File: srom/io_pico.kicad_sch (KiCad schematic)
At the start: 2 parts, among them J201 Conn_01x03_Female, U201 Pico-2 IO

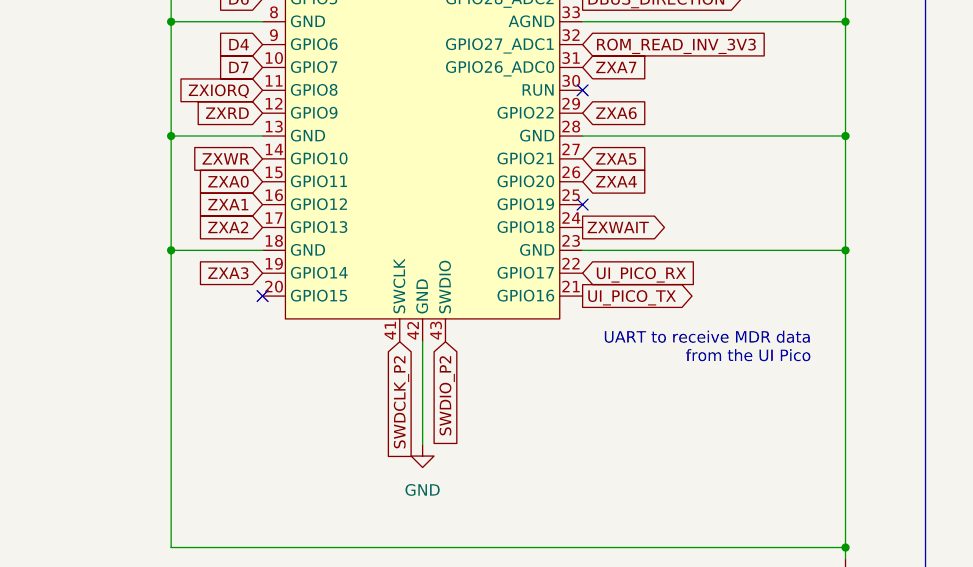
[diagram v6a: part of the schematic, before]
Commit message: move the ZXWAIT signal on pico2 off the SP1 connection. matches latest hardware
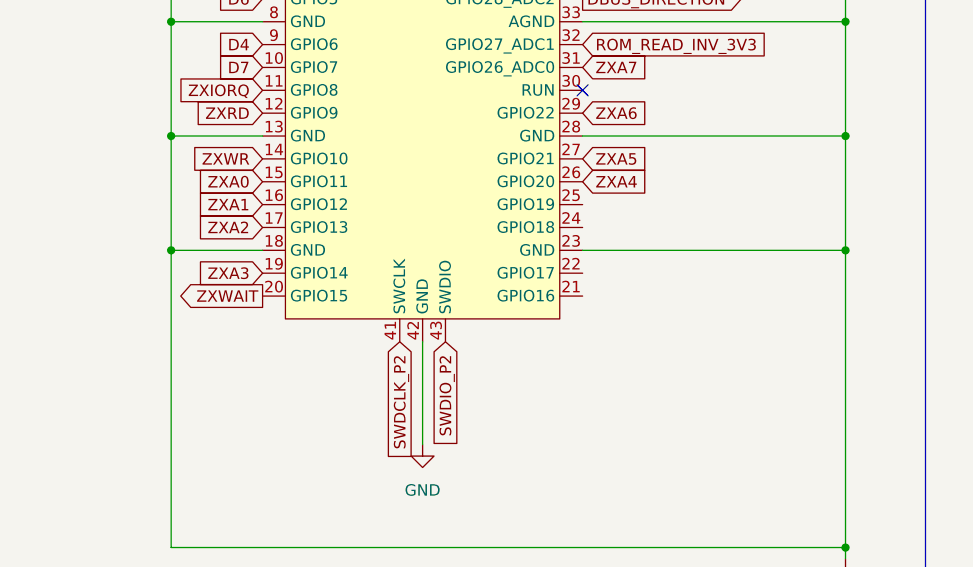
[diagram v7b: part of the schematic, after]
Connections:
- net ZXWAIT: now also U201.20 (GPIO15); no longer U201.24 (GPIO18)
- net UI_PICO_RX: no longer names the net of U201.22 (GPIO17)
- net UI_PICO_TX: no longer names the net of U201.21 (GPIO16)
- no-connect marks 6 -> 4
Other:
- note removed: "UART to receive MDR data from the UI Pico"
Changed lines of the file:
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@@
   )
   (no_connect (at 162.56 49.53))
-  (no_connect (at 127 97.79))
   (no_connect (at 162.56 62.23))
   (no_connect (at 162.56 57.15))
-  (no_connect (at 162.56 87.63))
   (no_connect (at 162.56 74.93))
   (polyline (pts (xy 95.25 155.575) (xy 95.25 35.56))
@@
     (stroke (width 0) (type default) (color 0 0 0 0))
   )
-  (text "UART to receive MDR data\nfrom the UI Pico" (at 187.96 105.41 180)
-    (effects (font (size 1.27 1.27)) (justify right bottom))
-  )
   (text "Pico watches the /IORQ waiting for a Z80 IN or OUT. It knows which from the /RD and /WR lines.\nIt only needs the lower 8 bits of the address bus, and loads the result onto the data bus lines.\n\nThis Pico does the data bus level shifter direction change for both a memory read and an IO\nread. The PIO program which changes the level shifter (BUS_DIRECTION) runs here. That's why\nROM_READ_INV is required as an input here.\n\n/WAIT is output from here to the Z80 when the Pico code needs the Z80 to wait while the byte\nfor the microdrive is dealt with.\n\nMDR data will come in from the UI Pico via UART.\n"
     (at 96.52 154.94 0)
@@
     (property "Intersheet References" "${INTERSHEET_REFS}" (id 0) (at 119.8698 85.0106 0)
       (effects (font (size 1.27 1.27)) (justify right) hide)
-    )
-  )
-  (global_label "UI_PICO_RX" (shape input) (at 162.56 95.25 0) (fields_autoplaced)
-    (effects (font (size 1.27 1.27)) (justify left))
-    (property "Intersheet References" "${INTERSHEET_REFS}" (id 0) (at 175.7983 95.1706 0)
-      (effects (font (size 1.27 1.27)) (justify left) hide)
     )
   )
@@
     (effects (font (size 1.27 1.27)) (justify left))
     (property "Intersheet References" "${INTERSHEET_REFS}" (id 0) (at 192.1874 51.9906 0)
-      (effects (font (size 1.27 1.27)) (justify left) hide)
-    )
-  )
-  (global_label "UI_PICO_TX" (shape output) (at 162.56 97.79 0) (fields_autoplaced)
-    (effects (font (size 1.27 1.27)) (justify left))
-    (property "Intersheet References" "${INTERSHEET_REFS}" (id 0) (at 175.496 97.7106 0)
       (effects (font (size 1.27 1.27)) (justify left) hide)
     )
@@
     )
   )
-  (global_label "ZXWAIT" (shape output) (at 162.56 90.17 0) (fields_autoplaced)
-    (effects (font (size 1.27 1.27)) (justify left))
-    (property "Intersheet References" "${INTERSHEET_REFS}" (id 0) (at 171.5045 90.0906 0)
-      (effects (font (size 1.27 1.27)) (justify left) hide)
+  (global_label "ZXWAIT" (shape output) (at 127 97.79 180) (fields_autoplaced)
+    (effects (font (size 1.27 1.27)) (justify right))
+    (property "Intersheet References" "${INTERSHEET_REFS}" (id 0) (at 118.0555 97.8694 0)
+      (effects (font (size 1.27 1.27)) (justify right) hide)
     )
   )

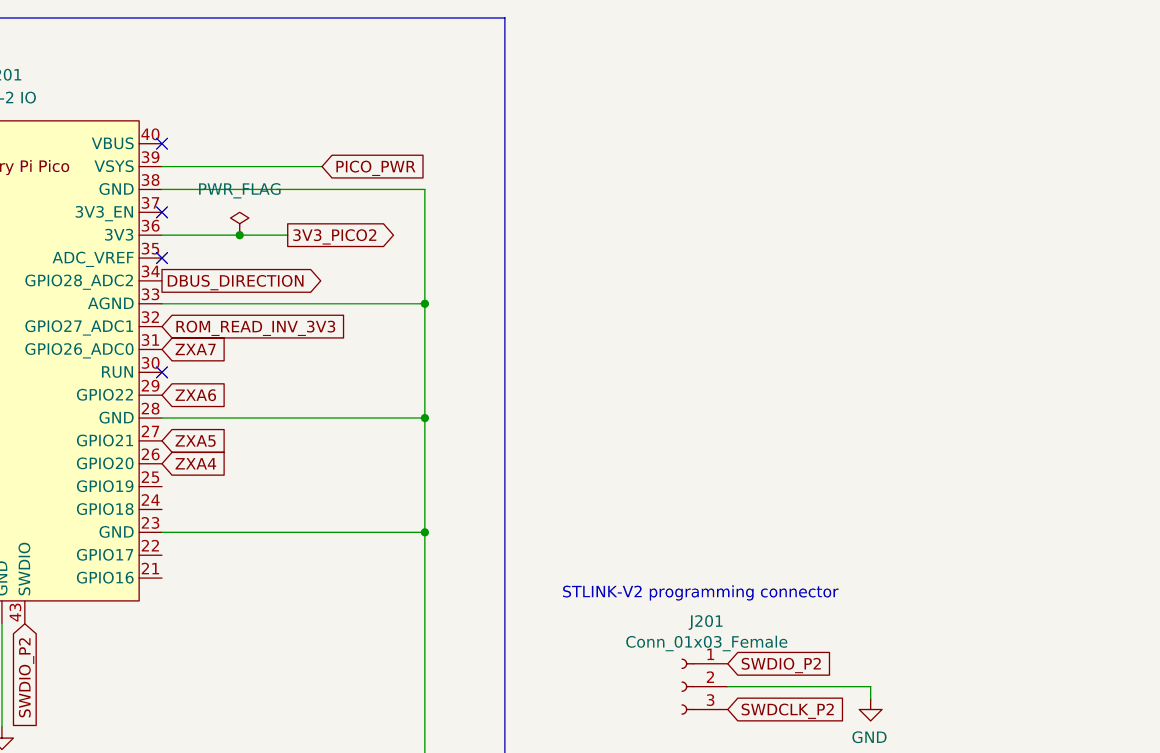
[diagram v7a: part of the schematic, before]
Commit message: update schematic to match current hardware
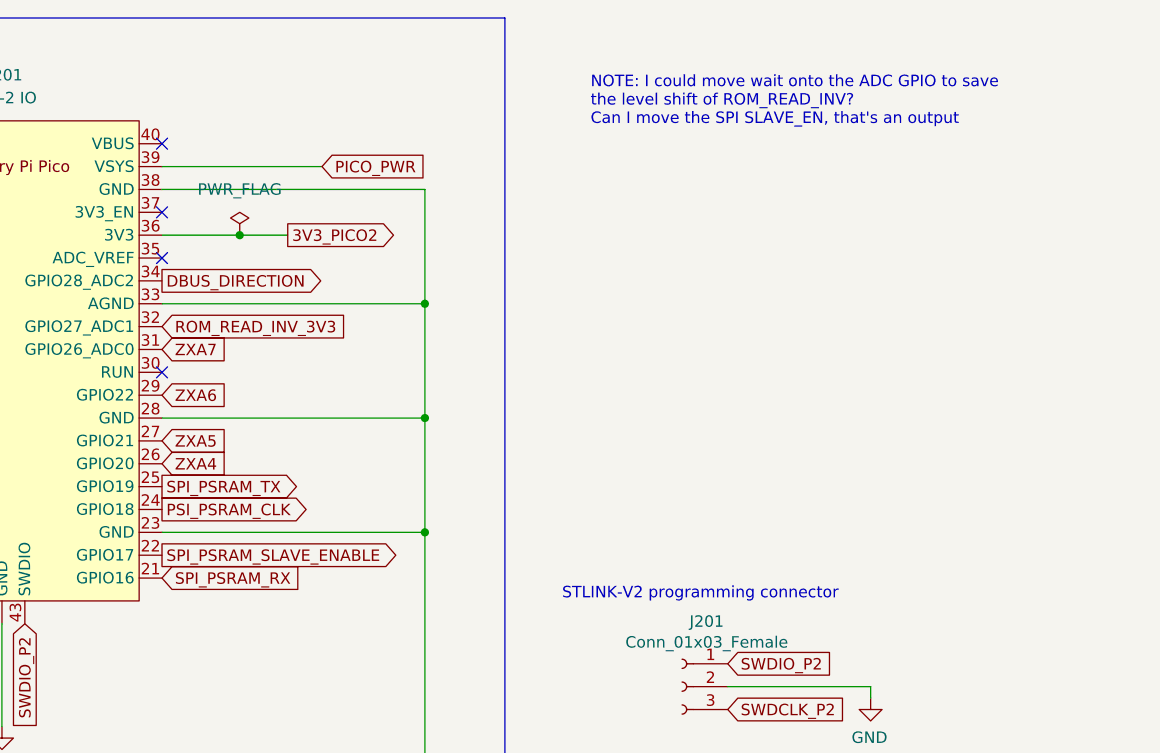
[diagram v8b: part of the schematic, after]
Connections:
- net SPI_PSRAM_RX: now reaches U201.21 (GPIO16)
- net SPI_PSRAM_SLAVE_ENABLE: now reaches U201.22 (GPIO17)
- net PSI_PSRAM_CLK: now reaches U201.24 (GPIO18)
- net SPI_PSRAM_TX: now reaches U201.25 (GPIO19)
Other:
- note added: "NOTE: I could move wait onto the ADC GPIO to save the level shift of ROM_READ_INV? Can I move the SPI SLAVE_EN, that's an output"
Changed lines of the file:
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@@
     (stroke (width 0) (type default) (color 0 0 0 0))
+  )
+  (text "NOTE: I could move wait onto the ADC GPIO to save\nthe level shift of ROM_READ_INV?\nCan I move the SPI SLAVE_EN, that's an output\n"
+    (at 210.185 47.625 0)
+    (effects (font (size 1.27 1.27)) (justify left bottom))
   )
   (text "Pico watches the /IORQ waiting for a Z80 IN or OUT. It knows which from the /RD and /WR lines.\nIt only needs the lower 8 bits of the address bus, and loads the result onto the data bus lines.\n\nThis Pico does the data bus level shifter direction change for both a memory read and an IO\nread. The PIO program which changes the level shifter (BUS_DIRECTION) runs here. That's why\nROM_READ_INV is required as an input here.\n\n/WAIT is output from here to the Z80 when the Pico code needs the Z80 to wait while the byte\nfor the microdrive is dealt with.\n\nMDR data will come in from the UI Pico via UART.\n"
@@
     )
   )
+  (global_label "PSI_PSRAM_CLK" (shape output) (at 162.56 90.17 0) (fields_autoplaced)
+    (effects (font (size 1.27 1.27)) (justify left))
+    (property "Intersheet References" "${INTERSHEET_REFS}" (id 0) (at 179.8502 90.0906 0)
+      (effects (font (size 1.27 1.27)) (justify left) hide)
+    )
+  )
   (global_label "3V3_PICO2" (shape output) (at 176.53 59.69 0) (fields_autoplaced)
     (effects (font (size 1.27 1.27)) (justify left))
@@
     (property "Intersheet References" "${INTERSHEET_REFS}" (id 0) (at 119.8698 90.0906 0)
       (effects (font (size 1.27 1.27)) (justify right) hide)
+    )
+  )
+  (global_label "SPI_PSRAM_TX" (shape output) (at 162.56 87.63 0) (fields_autoplaced)
+    (effects (font (size 1.27 1.27)) (justify left))
+    (property "Intersheet References" "${INTERSHEET_REFS}" (id 0) (at 178.4593 87.5506 0)
+      (effects (font (size 1.27 1.27)) (justify left) hide)
     )
   )
@@
     )
   )
+  (global_label "SPI_PSRAM_RX" (shape input) (at 162.56 97.79 0) (fields_autoplaced)
+    (effects (font (size 1.27 1.27)) (justify left))
+    (property "Intersheet References" "${INTERSHEET_REFS}" (id 0) (at 178.7617 97.7106 0)
+      (effects (font (size 1.27 1.27)) (justify left) hide)
+    )
+  )
   (global_label "ROM_READ_INV_3V3" (shape input) (at 162.56 69.85 0) (fields_autoplaced)
     (effects (font (size 1.27 1.27)) (justify left))
@@
       (effects (font (size 1.27 1.27)) (justify left) hide)
     )
+  )
+  (global_label "SPI_PSRAM_SLAVE_ENABLE" (shape output) (at 162.56 95.25 0) (fields_autoplaced)
+    (effects (font (size 1.27 1.27)) (justify left))
+    (property "Intersheet References" "${INTERSHEET_REFS}" (id 0) (at 189.8288 95.1706 0)
+      (effects (font (size 1.27 1.27)) (justify left) hide)
+    )
